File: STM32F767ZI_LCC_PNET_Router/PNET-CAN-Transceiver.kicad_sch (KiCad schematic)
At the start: 15 parts, among them J301 Termination, J302 PNET, J303 PNET, T401 PNet Power In, U301 LM358, U302 TCAN332DR

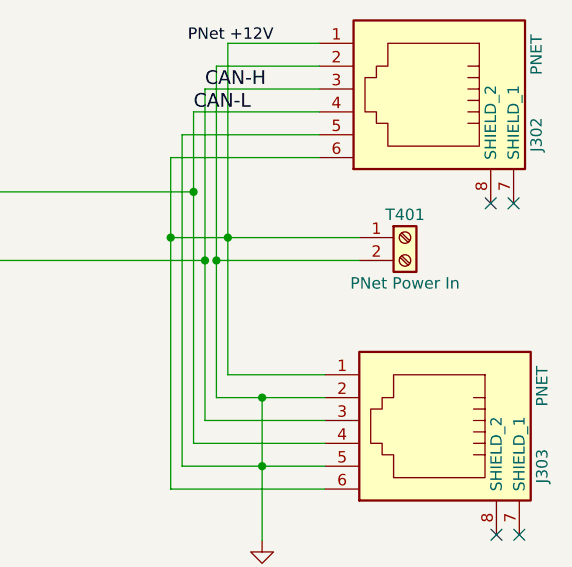
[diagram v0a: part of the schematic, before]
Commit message: Add plus signs to power terminal marking (show polarity).
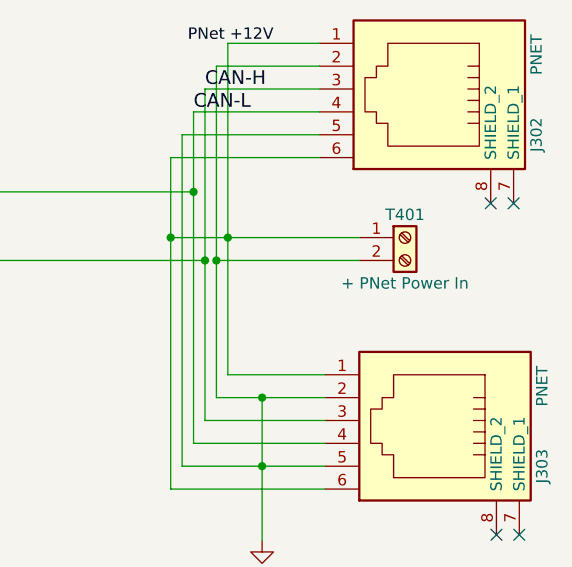
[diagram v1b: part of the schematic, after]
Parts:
- T401: value PNet Power In -> + PNet Power In
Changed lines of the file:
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@@
     (in_bom yes) (on_board yes)
     (property "Reference" "T401" (id 0) (at 200.025 73.66 0))
-    (property "Value" "PNet Power In" (id 1) (at 200.025 81.28 0))
+    (property "Value" "+ PNet Power In" (id 1) (at 200.025 81.28 0))
     (property "Footprint" "TerminalBlock_TE-Connectivity:TerminalBlock_TE_282834-2_1x02_P2.54mm_Horizontal" (id 2) (at 200.025 76.2 0)
       (effects (font (size 1.27 1.27)) hide)
